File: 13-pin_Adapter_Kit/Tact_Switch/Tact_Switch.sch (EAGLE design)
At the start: 3 parts

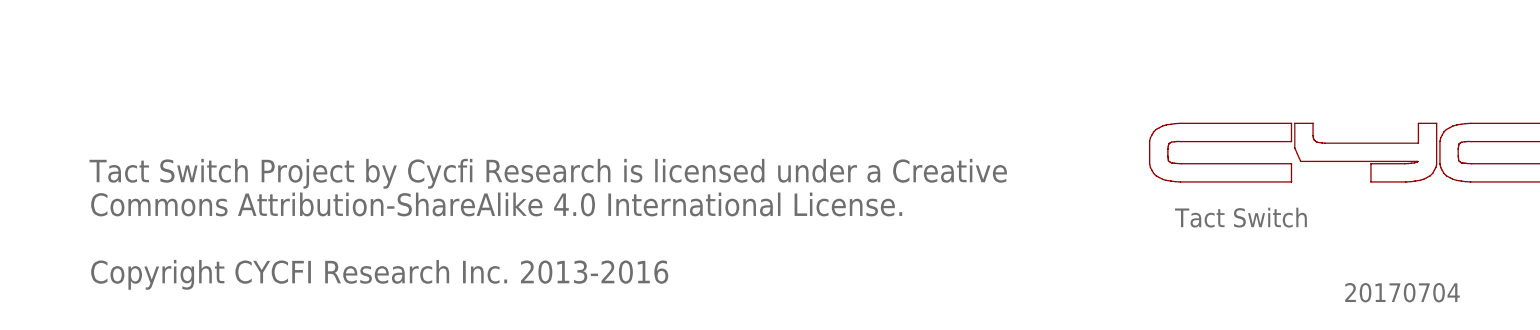
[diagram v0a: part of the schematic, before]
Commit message: Updated Notes "For Nu Project" instead of "Nexus"
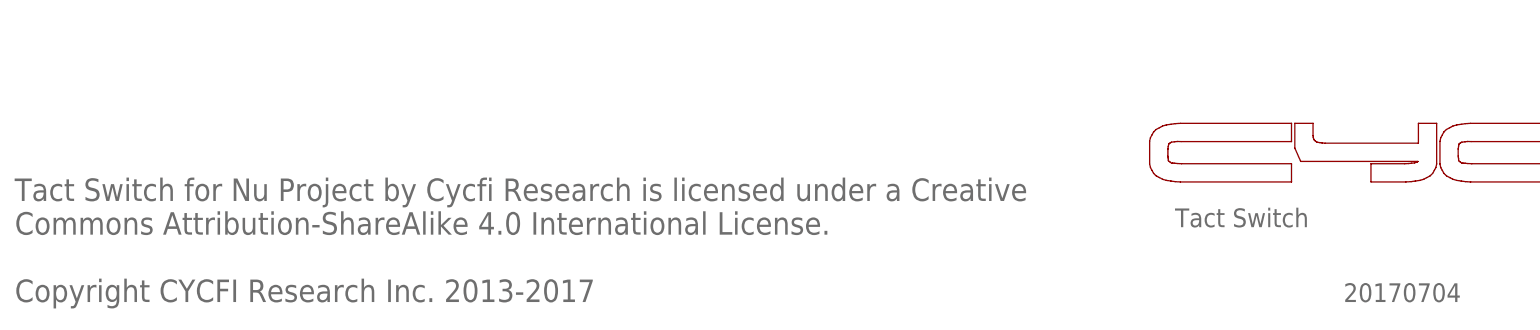
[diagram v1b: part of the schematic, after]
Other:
- note added: "Tact Switch for Nu Project by Cycfi Research is licensed under a Creative Commons Attribution-ShareAlike 4.0 International License. Copyright CYCFI Research Inc. 2013-2017"
- note removed: "Tact Switch Project by Cycfi Research is licensed under a Creative Commons Attribution-ShareAlike 4.0 International License. Copyright CYCFI Research Inc. 2013-2016"
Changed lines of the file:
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@@
 <?xml version="1.0" encoding="utf-8"?>
 <!DOCTYPE eagle SYSTEM "eagle.dtd">
-<eagle version="6.3">
+<eagle version="7.6.0">
 <drawing>
 <settings>
@@
 <sheet>
 <plain>
-<text x="15.24" y="11.43" size="3.048" layer="95">Tact Switch Project by Cycfi Research is licensed under a Creative
+<text x="5.08" y="8.89" size="3.048" layer="95">Tact Switch for Nu Project by Cycfi Research is licensed under a Creative
 Commons Attribution-ShareAlike 4.0 International License.
-Copyright CYCFI Research Inc. 2013-2016</text>
+Copyright CYCFI Research Inc. 2013-2017</text>
 <text x="162.56" y="19.05" size="2.54" layer="95">Tact Switch</text>
 <wire x1="178.362721875" y1="25.186403125" x2="163.27975" y2="25.186403125" width="0" layer="94"/>

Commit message: Updated document number.
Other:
- note added: "0.9"
- note added: "2017024"
- note removed: "20170704"
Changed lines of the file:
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@@
 <sheet>
 <plain>
-<text x="5.08" y="8.89" size="3.048" layer="95">Tact Switch for Nu Project by Cycfi Research is licensed under a Creative
+<text x="5.08" y="8.89" size="2.54" layer="95">Tact Switch for Nu Project by Cycfi Research is licensed under a Creative
 Commons Attribution-ShareAlike 4.0 International License.
 Copyright CYCFI Research Inc. 2013-2017</text>
@@
 <text x="96.52" y="91.44" size="1.778" layer="95" rot="R180">SW1</text>
 <text x="134.62" y="91.44" size="1.778" layer="95" rot="R180">SW2</text>
-<text x="185.42" y="8.89" size="2.54" layer="95">20170704</text>
+<text x="185.42" y="8.89" size="2.54" layer="95">2017024</text>
+<text x="238.76" y="6.35" size="2.54" layer="95">0.9</text>
 </plain>
 <instances>
